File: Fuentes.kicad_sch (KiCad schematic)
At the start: 13 parts, among them J20 Conector 3V3, J21 Conector GND, J43 Conector GND, U1 LM2596S-5, U2 LM1117-3.3

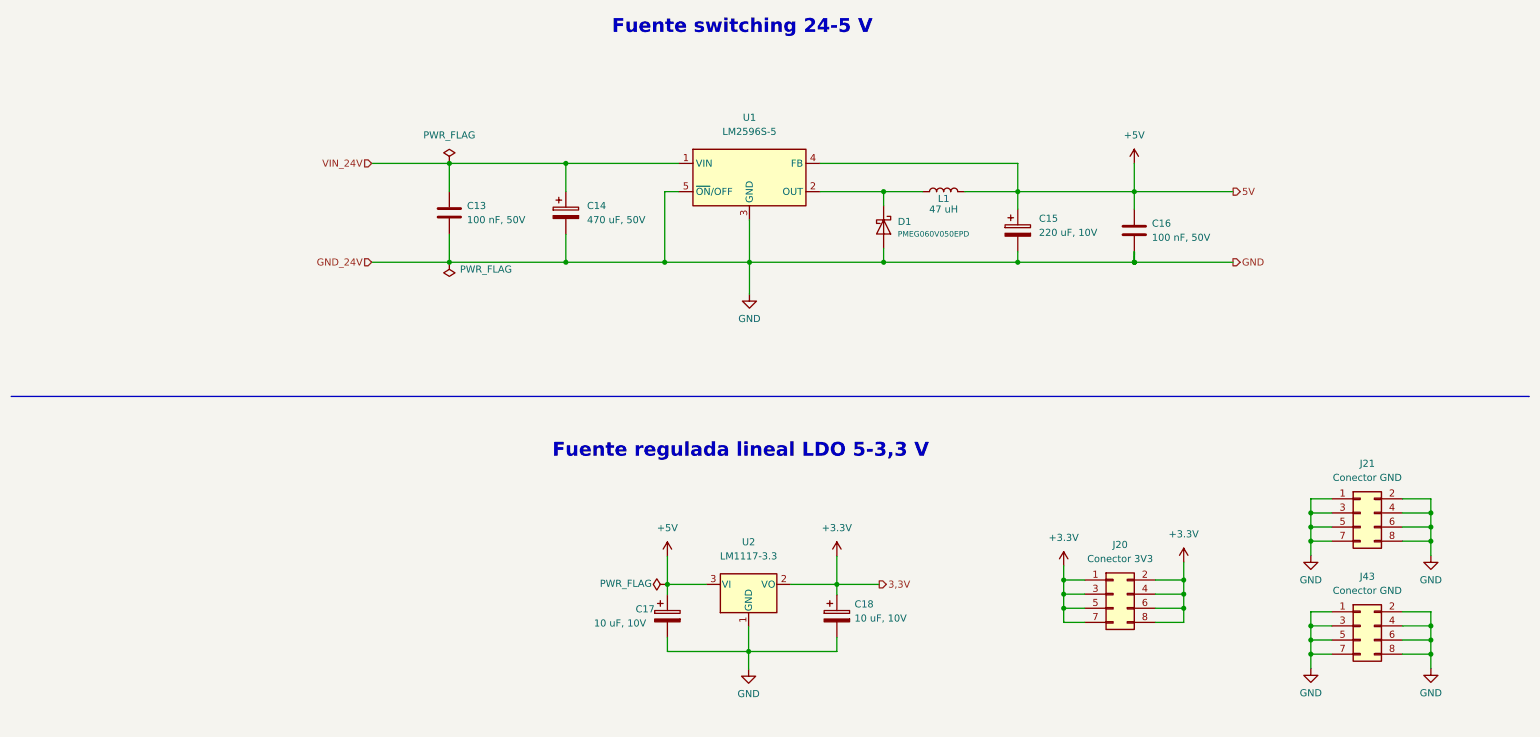
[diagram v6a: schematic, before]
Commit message: Se modificaron algunos componentes, según disponibilidad
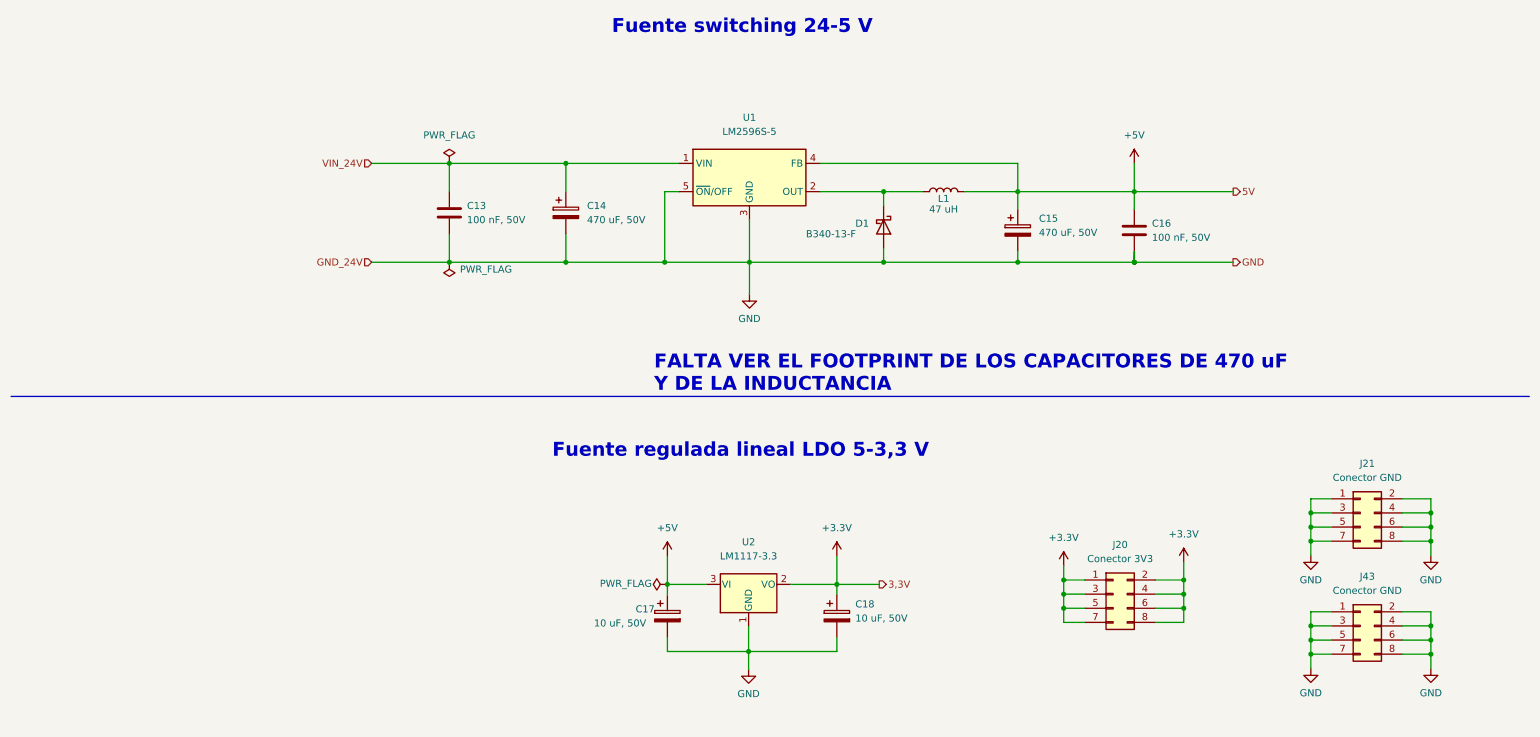
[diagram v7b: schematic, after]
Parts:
- removed D1: PMEG060V050EPD, Package_TO_SOT_SMD:Nexperia_CFP15_SOT-1289, symbol Diode:PMEG060V050EPD
- added D1: B340-13-F, B340-13-F:DIOM7959X250N, symbol Device:D_Schottky
- C15: value 220 uF, 10V -> 470 uF, 50V
- C17, C18: value 10 uF, 10V -> 10 uF, 50V
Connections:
- net GND: now also D1.2 (A)
- net at L1.1, U1.2 (OUT): now also D1.1 (K)
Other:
- note added: "FALTA VER EL FOOTPRINT DE LOS CAPACITORES DE 470 uF Y DE LA INDUCTANCIA"
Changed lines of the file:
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@@
+    (effects (font (size 2.5 2.5) (thickness 0.4) bold) (justify left bottom))
+  )
+  (text "FALTA VER EL FOOTPRINT DE LOS CAPACITORES DE 470 uF\nY DE LA INDUCTANCIA"
+    (at 127.635 90.805 0)
     (effects (font (size 2.5 2.5) (thickness 0.4) bold) (justify left bottom))
   )
@@
     (pin "2")
   )
-  (symbol (lib_id "Diode:PMEG060V050EPD") (at 168.91 60.96 270) (unit 1)
-    (in_bom yes) (on_board yes)
-    (property "Reference" "D1" (id 0) (at 171.45 60.0074 90)
-      (effects (font (size 1.27 1.27)) (justify left))
-    )
-    (property "Value" "PMEG060V050EPD" (id 1) (at 171.45 62.23 90)
-      (effects (font (size 1 1)) (justify left))
-    )
-    (property "Footprint" "Package_TO_SOT_SMD:Nexperia_CFP15_SOT-1289" (id 2) (at 164.465 60.96 0)
-      (effects (font (size 1.27 1.27)) hide)
-    )
-    (property "Datasheet" "https://assets.nexperia.com/documents/data-sheet/PMEG060V050EPD.pdf" (id 3) (at 168.91 60.96 0)
-      (effects (font (size 1.27 1.27)) hide)
-    )
-    (pin "1")
-    (pin "2")
-    (pin "3")
-  )
   (symbol (lib_id "power:GND") (at 267.335 140.335 0) (unit 1)
     (in_bom yes) (on_board yes) (fields_autoplaced)
@@
     (pin "2")
   )
+  (symbol (lib_id "Device:D_Schottky") (at 168.91 60.96 270) (unit 1)
+    (in_bom yes) (on_board yes)
+    (property "Reference" "D1" (id 0) (at 163.83 60.325 90)
+      (effects (font (size 1.27 1.27)) (justify left))
+    )
+    (property "Value" "B340-13-F" (id 1) (at 154.94 62.23 90)
+      (effects (font (size 1.27 1.27)) (justify left))
+    )
+    (property "Footprint" "B340-13-F:DIOM7959X250N" (id 2) (at 168.91 60.96 0)
+      (effects (font (size 1.27 1.27)) hide)
+    )
+    (property "Datasheet" "~" (id 3) (at 168.91 60.96 0)
+      (effects (font (size 1.27 1.27)) hide)
+    )
+    (pin "1")
+    (pin "2")
+  )
   (symbol (lib_id "Device:C_Polarized") (at 160.5026 130.9624 0) (unit 1)
     (in_bom yes) (on_board yes) (fields_autoplaced)
-    (property "Reference" "C18" (id 0) (at 163.6776 128.8033 0)
-      (effects (font (size 1.27 1.27)) (justify left))
-    )
-    (property "Value" "10 uF, 10V" (id 1) (at 163.6776 131.3433 0)
+    (property "Reference" "C18" (id 0) (at 163.83 128.8033 0)
+      (effects (font (size 1.27 1.27)) (justify left))
+    )
+    (property "Value" "10 uF, 50V" (id 1) (at 163.83 131.3433 0)
       (effects (font (size 1.27 1.27)) (justify left))
     )
@@
       (effects (font (size 1.27 1.27)) (justify left))
     )
-    (property "Value" "10 uF, 10V" (id 1) (at 126.2126 132.2324 0)
+    (property "Value" "10 uF, 50V" (id 1) (at 126.2126 132.2324 0)
       (effects (font (size 1.27 1.27)) (justify right))
     )
@@
       (effects (font (size 1.27 1.27)) (justify left))
     )
-    (property "Value" "220 uF, 10V" (id 1) (at 196.85 61.9759 0)
-      (effects (font (size 1.27 1.27)) (justify left))
-    )
+    (property "Value" "470 uF, 50V" (id 1) (at 196.85 61.9759 0)
+      (effects (font (size 1.27 1.27)) (justify left))
+    )

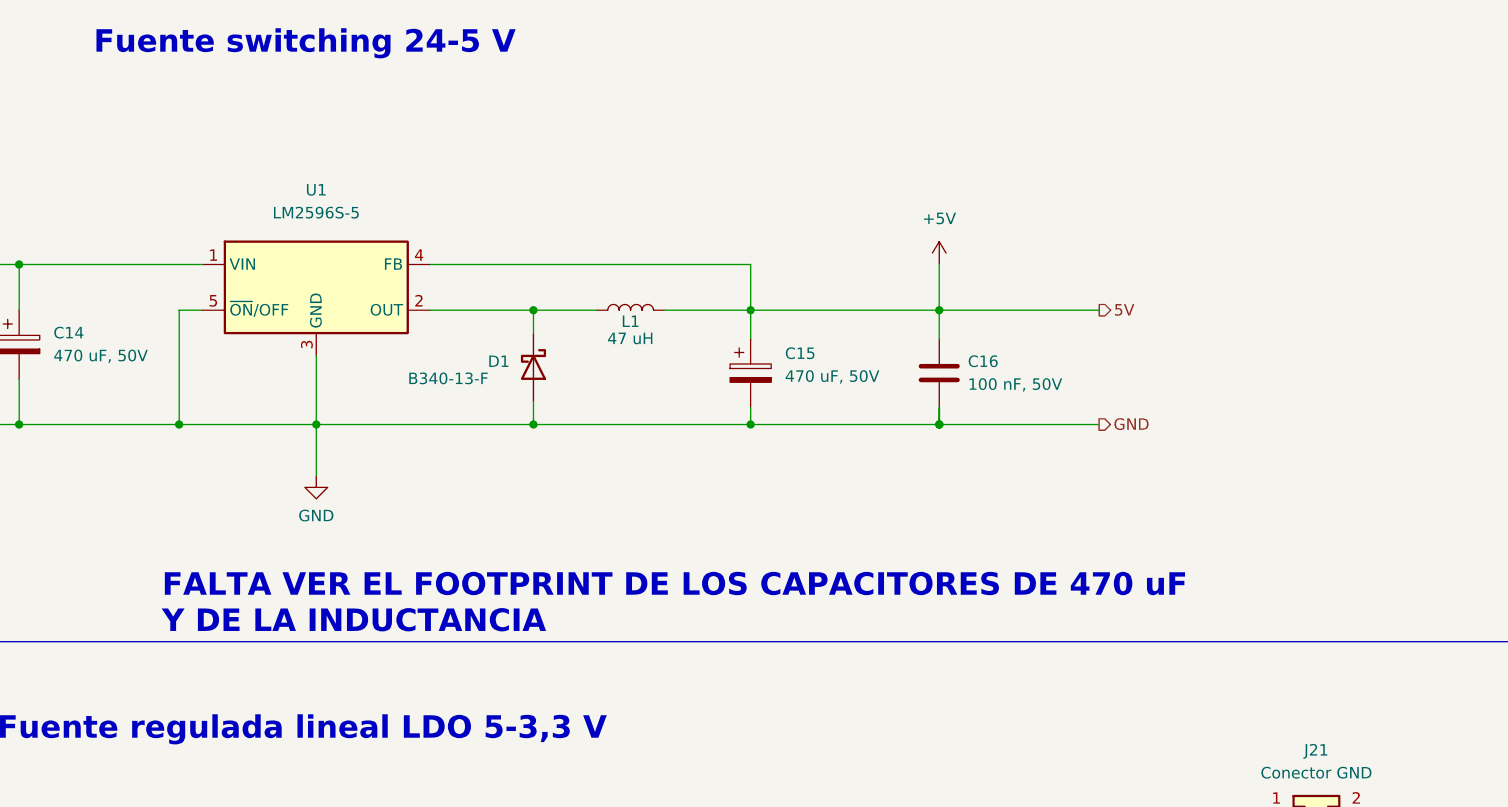
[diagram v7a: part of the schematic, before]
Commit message: Correccion footprints
Se realizo el cambio de algunas footprints segun los componentes disponibles, como los capacitores de 470 uF o la inductancia de la fte switching, y tambien se cambio el LM2596 por el modelo ADJ, con el agregado de un divisor resistivo.
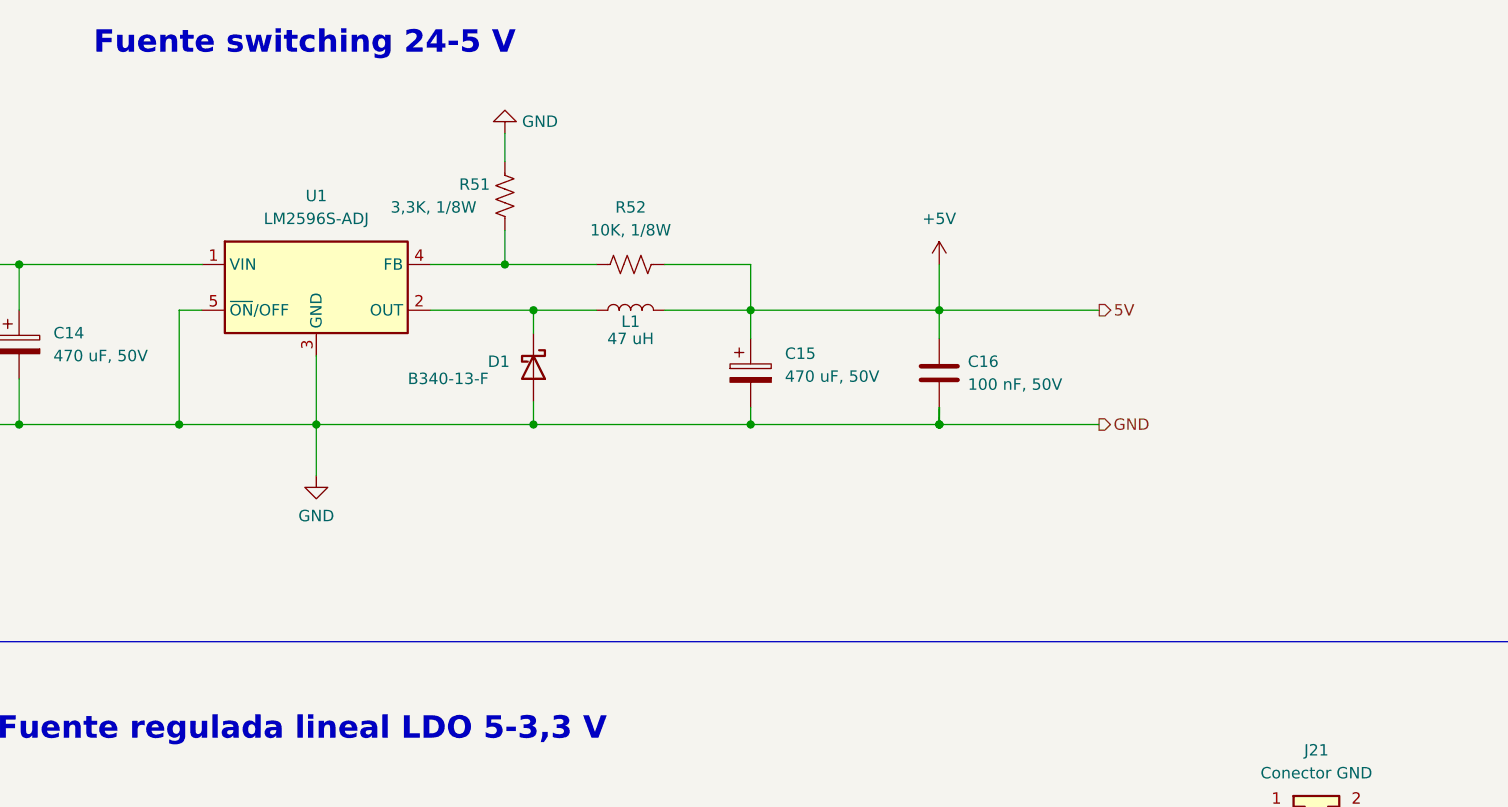
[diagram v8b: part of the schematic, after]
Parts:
- removed U1: LM2596S-5, Package_TO_SOT_SMD:TO-263-5_TabPin3, symbol Regulator_Switching:LM2596S-5
- added R51: 3,3K, 1/8W, Resistor_SMD:R_0805_2012Metric, symbol Device:R_US
- added R52: 10K, 1/8W, Resistor_SMD:R_0805_2012Metric, symbol Device:R_US
- added U1: LM2596S-ADJ, LM2596SX-ADJ_NOPB:LM2596SXADJNOPB, symbol Regulator_Switching:LM2596S-ADJ
- C14: footprint VE-471M1HTR-1316:CAPAE1300X1650N -> Capacitor_THT:CP_Radial_D10.0mm_P5.00mm
- C15: footprint TPSE227K010R0100:TPSE227K016R0100V -> Capacitor_THT:CP_Radial_D10.0mm_P5.00mm
- C17, C18: footprint Capacitor_SMD:C_0805_2012Metric -> Capacitor_THT:CP_Radial_D5.0mm_P2.00mm
- L1: footprint 7447709470:WE-PD_1260_1245_1280_121054 -> Inductor_THT:L_Radial_D7.5mm_P5.00mm_Fastron_07P
- U2: footprint LM1117SX-3V3-NOPB:KTT0003B -> LM1117MPX-33NOPB:SOT230P700X180-4N
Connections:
- net +5V: now also R52.2
- net GND: now also R51.1, U1.3 (GND), U1.5 (~{ON}/OFF)
- net VIN_24V: now also U1.1 (VIN)
- net at D1.1 (K), L1.1: now also U1.2 (OUT)
- new net: R51.2, R52.1, U1.4 (FB)
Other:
- note removed: "FALTA VER EL FOOTPRINT DE LOS CAPACITORES DE 470 uF Y DE LA INDUCTANCIA"
